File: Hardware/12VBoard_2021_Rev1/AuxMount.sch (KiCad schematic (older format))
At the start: 27 parts, among them Q4 CSD18537NQ5A, Q5 CSD18531Q5A, U10 LM5116, U11 INA198

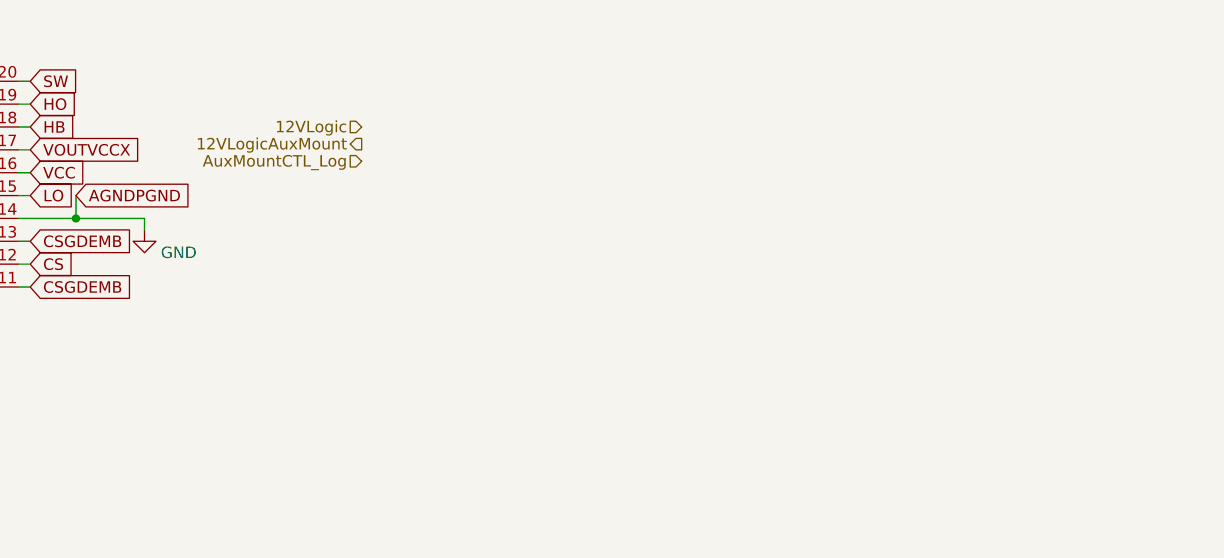
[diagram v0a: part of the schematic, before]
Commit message: Added Mosfet cicuitry to turn on/off logic power for high current side
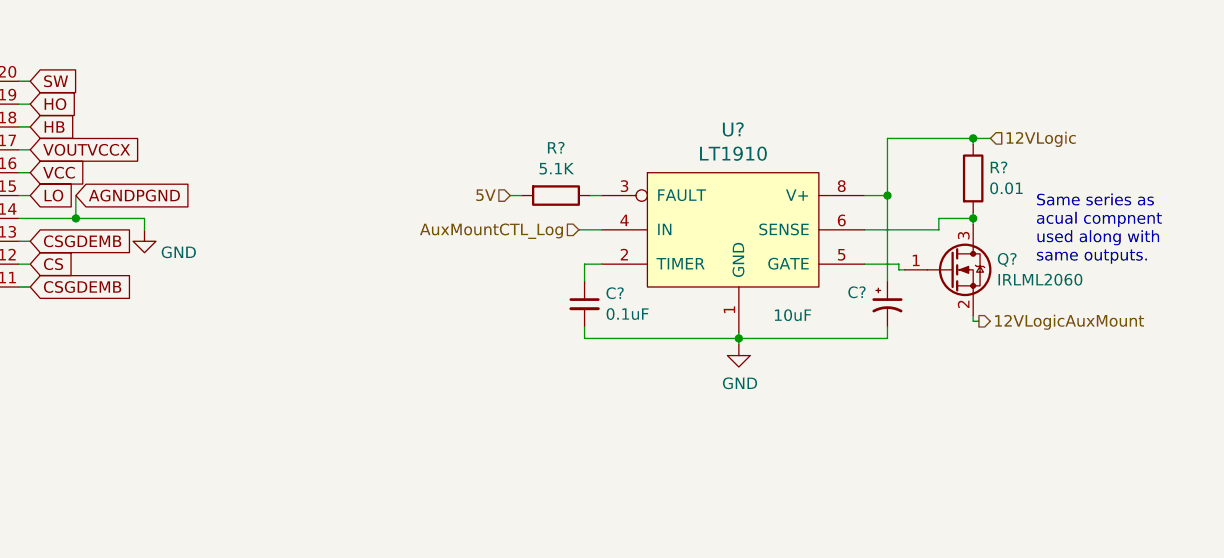
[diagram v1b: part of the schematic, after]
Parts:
- added C?: 0.1uF, symbol Device:C_Small
- added C?: 10uF, symbol Device:CP1_Small
- added Q?: IRLML2060, Package_TO_SOT_SMD:SOT-23, symbol Transistor_FET:IRLML2060
- added R?: 0.01, symbol Device:R
- added R?: 5.1K, symbol Device:R
- added U?: LT1910, symbol MRDT_ICs:LT1910
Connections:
- net 12VLogic: now also C?.1, R?.1, U?.8 (V+)
- net 12VLogicAuxMount: now also Q?.2 (S)
- net 5V: now also R?.2
- net AuxMountCTL_Log: now also U?.4 (IN)
- net GND: now also C?.2, C?.2, U?.1 (GND)
- new net: C?.1, U?.2 (TIMER)
- new net: R?.1, U?.3 (FAULT)
- new net: Q?.1 (G), U?.5 (GATE)
- new net: Q?.3 (D), R?.2, U?.6 (SENSE)
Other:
- note added: "Same series as \nacual compnent\nused along with\nsame outputs."
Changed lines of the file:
@@
 Wire Wire Line
 	1000 1100 1000 1175
-Text HLabel 5000 1000 0    50   Input ~ 0
+Text HLabel 7700 1850 2    50   Output ~ 0
+12VLogicAuxMount
+Text HLabel 5950 1450 0    50   Input ~ 0
+AuxMountCTL_Log
+Text HLabel 7750 1050 2    50   Input ~ 0
 12VLogic
-Text HLabel 5000 1075 0    50   Output ~ 0
-12VLogicAuxMount
-Text HLabel 5000 1150 0    50   Input ~ 0
-AuxMountCTL_Log
+$Comp
+L MRDT_ICs:LT1910 U?
+U 1 1 5FC2DAD4
+P 6250 1700
+AR Path="/5F74F36B/5F971CD6/5FC2DAD4" Ref="U?"  Part="1"
+AR Path="/5F74F36B/5F8222BE/5FC2DAD4" Ref="U?"  Part="1"
+F 0 "U?" H 6625 2387 60  0000 C CNN
+F 1 "LT1910" H 6625 2281 60  0000 C CNN
+F 2 "" H 6250 1700 60  0001 C CNN
+F 3 "" H 6250 1700 60  0001 C CNN
+	1    6250 1700
+	1    0    0    -1
+$EndComp
+$Comp
+L Device:C_Small C?
+U 1 1 5FC2DADA
+P 5975 1775
+AR Path="/5F74F36B/5F971CD6/5FC2DADA" Ref="C?"  Part="1"
+AR Path="/5F74F36B/5F8222BE/5FC2DADA" Ref="C?"  Part="1"
+F 0 "C?" H 6067 1821 50  0000 L CNN
+F 1 "0.1uF" H 6067 1730 50  0000 L CNN
+F 2 "" H 5975 1775 50  0001 C CNN
+F 3 "~" H 5975 1775 50  0001 C CNN
+	1    5975 1775
+	1    0    0    -1
+$EndComp
+$Comp
+L Device:CP1_Small C?
+U 1 1 5FC2DAE0
+P 7300 1775
+AR Path="/5F74F36B/5F971CD6/5FC2DAE0" Ref="C?"  Part="1"
+AR Path="/5F74F36B/5F8222BE/5FC2DAE0" Ref="C?"  Part="1"
+F 0 "C?" H 7125 1825 50  0000 L CNN
+F 1 "10uF" H 6800 1725 50  0000 L CNN
+F 2 "" H 7300 1775 50  0001 C CNN
+F 3 "~" H 7300 1775 50  0001 C CNN
+	1    7300 1775
+	1    0    0    -1
+$EndComp
+$Comp
+L power:GND #PWR?
+U 1 1 5FC2DAE6
+P 6650 1950
+AR Path="/5F74F36B/5F971CD6/5FC2DAE6" Ref="#PWR?"  Part="1"
+AR Path="/5F74F36B/5F8222BE/5FC2DAE6" Ref="#PWR?"  Part="1"
+F 0 "#PWR?" H 6650 1700 50  0001 C CNN
+F 1 "GND" H 6655 1777 50  0000 C CNN
+F 2 "" H 6650 1950 50  0001 C CNN
+F 3 "" H 6650 1950 50  0001 C CNN
+	1    6650 1950
+	1    0    0    -1
+$EndComp
+Wire Wire Line
+	6650 1900 6650 1925
+Wire Wire Line
+	6650 1950 6650 1925
+Connection ~ 6650 1925
+Wire Wire Line
+	6650 1925 5975 1925
+Wire Wire Line
+	5975 1925 5975 1875
+Wire Wire Line
+	7300 1875 7300 1925
+Wire Wire Line
+	6650 1925 7300 1925
+Wire Wire Line
+	7300 1675 7300 1300
+Wire Wire Line
+	7300 1300 7200 1300
+Wire Wire Line
+	6050 1600 5975 1600
+Wire Wire Line
+	5975 1600 5975 1675
+Wire Wire Line
+	6000 1300 6050 1300
+$Comp
+L Transistor_FET:IRLML2060 Q?
+U 1 1 5FC2DB00
+P 7575 1625
+AR Path="/5F74F36B/5F971CD6/5FC2DB00" Ref="Q?"  Part="1"
+AR Path="/5F74F36B/5F8222BE/5FC2DB00" Ref="Q?"  Part="1"
+F 0 "Q?" H 7779 1671 50  0000 L CNN
+F 1 "IRLML2060" H 7779 1580 50  0000 L CNN
+F 2 "Package_TO_SOT_SMD:SOT-23" H 7775 1550 50  0001 L CIN
+F 3 "https://www.infineon.com/dgdl/irlml2060pbf.pdf?fileId=5546d462533600a401535664b7fb25ee" H 7575 1625 50  0001 L CNN
+	1    7575 1625
+	1    0    0    -1
+$EndComp
+Wire Wire Line
+	7200 1450 7525 1450
+Wire Wire Line
+	7525 1450 7525 1400
+Wire Wire Line
+	7525 1400 7675 1400
+Wire Wire Line
+	7675 1400 7675 1375
+Wire Wire Line
+	7675 1400 7675 1425
+Connection ~ 7675 1400
+Wire Wire Line
+	7300 1300 7300 1050
+Wire Wire Line
+	7300 1050 7675 1050
+Wire Wire Line
+	7675 1050 7675 1075
+Connection ~ 7300 1300
+Wire Wire Line
+	7700 1850 7675 1850
+Wire Wire Line
+	7675 1850 7675 1825
+Connection ~ 7675 1050
+Wire Wire Line
+	7675 1050 7750 1050
+Wire Wire Line
+	5950 1450 6050 1450
+Wire Wire Line
+	7375 1625 7350 1625
+Wire Wire Line
+	7350 1625 7350 1600
+Wire Wire Line
+	7350 1600 7200 1600
+Text Notes 7950 1600 0    50   ~ 0
+Same series as \nacual compnent\nused along with\nsame outputs.
+$Comp
+L Device:R R?
+U 1 1 5FC2DB1B
+P 7675 1225
+AR Path="/5F74F36B/5F971CD6/5FC2DB1B" Ref="R?"  Part="1"
+AR Path="/5F74F36B/5F8222BE/5FC2DB1B" Ref="R?"  Part="1"
+F 0 "R?" H 7745 1271 50  0000 L CNN
+F 1 "0.01" H 7745 1180 50  0000 L CNN
+F 2 "" V 7605 1225 50  0001 C CNN
+F 3 "~" H 7675 1225 50  0001 C CNN
+	1    7675 1225
+	1    0    0    -1
+$EndComp
+$Comp
+L Device:R R?
+U 1 1 5FC2DB21
+P 5850 1300
+AR Path="/5F74F36B/5F971CD6/5FC2DB21" Ref="R?"  Part="1"
+AR Path="/5F74F36B/5F8222BE/5FC2DB21" Ref="R?"  Part="1"
+F 0 "R?" V 5643 1300 50  0000 C CNN
+F 1 "5.1K" V 5734 1300 50  0000 C CNN
+F 2 "" V 5780 1300 50  0001 C CNN
+F 3 "~" H 5850 1300 50  0001 C CNN
+	1    5850 1300
+	0    1    1    0
+$EndComp
+Text HLabel 5650 1300 0    50   Input ~ 0
+5V
+Wire Wire Line
+	5650 1300 5700 1300
 $EndSCHEMATC

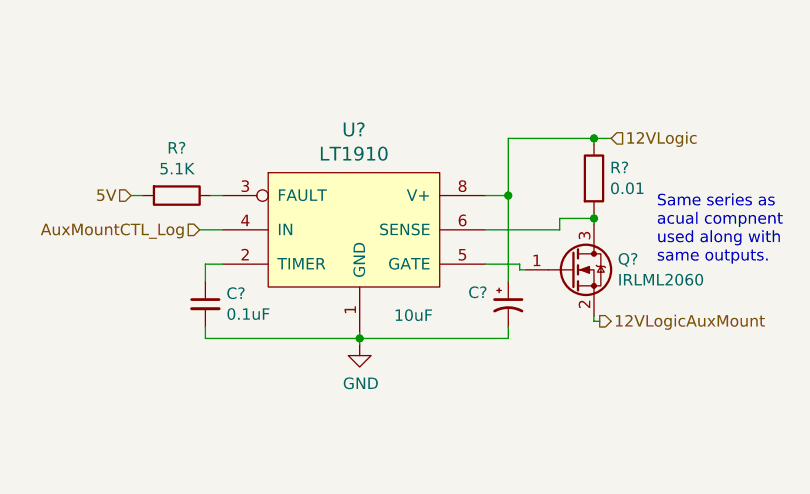
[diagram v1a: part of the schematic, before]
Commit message: Redesigned low current ports schematic
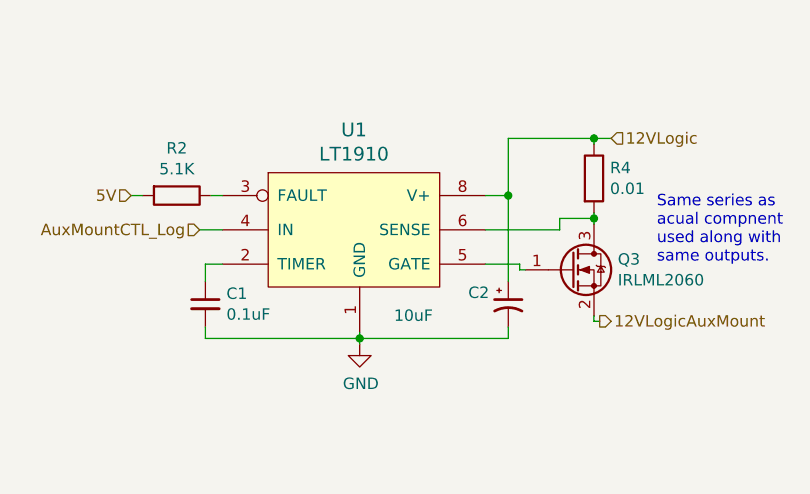
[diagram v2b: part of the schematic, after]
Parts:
- gave numbers to parts that had none: 6
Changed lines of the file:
@@
 P 6250 1700
 AR Path="/5F74F36B/5F971CD6/5FC2DAD4" Ref="U?"  Part="1"
-AR Path="/5F74F36B/5F8222BE/5FC2DAD4" Ref="U?"  Part="1"
-F 0 "U?" H 6625 2387 60  0000 C CNN
+AR Path="/5F74F36B/5F8222BE/5FC2DAD4" Ref="U1"  Part="1"
+F 0 "U1" H 6625 2387 60  0000 C CNN
 F 1 "LT1910" H 6625 2281 60  0000 C CNN
 F 2 "" H 6250 1700 60  0001 C CNN
@@
 P 5975 1775
 AR Path="/5F74F36B/5F971CD6/5FC2DADA" Ref="C?"  Part="1"
-AR Path="/5F74F36B/5F8222BE/5FC2DADA" Ref="C?"  Part="1"
-F 0 "C?" H 6067 1821 50  0000 L CNN
+AR Path="/5F74F36B/5F8222BE/5FC2DADA" Ref="C1"  Part="1"
+F 0 "C1" H 6067 1821 50  0000 L CNN
 F 1 "0.1uF" H 6067 1730 50  0000 L CNN
 F 2 "" H 5975 1775 50  0001 C CNN
@@
 P 7300 1775
 AR Path="/5F74F36B/5F971CD6/5FC2DAE0" Ref="C?"  Part="1"
-AR Path="/5F74F36B/5F8222BE/5FC2DAE0" Ref="C?"  Part="1"
-F 0 "C?" H 7125 1825 50  0000 L CNN
+AR Path="/5F74F36B/5F8222BE/5FC2DAE0" Ref="C2"  Part="1"
+F 0 "C2" H 7125 1825 50  0000 L CNN
 F 1 "10uF" H 6800 1725 50  0000 L CNN
 F 2 "" H 7300 1775 50  0001 C CNN
@@
 P 6650 1950
 AR Path="/5F74F36B/5F971CD6/5FC2DAE6" Ref="#PWR?"  Part="1"
-AR Path="/5F74F36B/5F8222BE/5FC2DAE6" Ref="#PWR?"  Part="1"
-F 0 "#PWR?" H 6650 1700 50  0001 C CNN
+AR Path="/5F74F36B/5F8222BE/5FC2DAE6" Ref="#PWR01"  Part="1"
+F 0 "#PWR01" H 6650 1700 50  0001 C CNN
 F 1 "GND" H 6655 1777 50  0000 C CNN
 F 2 "" H 6650 1950 50  0001 C CNN
@@
 P 7575 1625
 AR Path="/5F74F36B/5F971CD6/5FC2DB00" Ref="Q?"  Part="1"
-AR Path="/5F74F36B/5F8222BE/5FC2DB00" Ref="Q?"  Part="1"
-F 0 "Q?" H 7779 1671 50  0000 L CNN
+AR Path="/5F74F36B/5F8222BE/5FC2DB00" Ref="Q3"  Part="1"
+F 0 "Q3" H 7779 1671 50  0000 L CNN
 F 1 "IRLML2060" H 7779 1580 50  0000 L CNN
 F 2 "Package_TO_SOT_SMD:SOT-23" H 7775 1550 50  0001 L CIN
@@
 P 7675 1225
 AR Path="/5F74F36B/5F971CD6/5FC2DB1B" Ref="R?"  Part="1"
-AR Path="/5F74F36B/5F8222BE/5FC2DB1B" Ref="R?"  Part="1"
-F 0 "R?" H 7745 1271 50  0000 L CNN
+AR Path="/5F74F36B/5F8222BE/5FC2DB1B" Ref="R4"  Part="1"
+F 0 "R4" H 7745 1271 50  0000 L CNN
 F 1 "0.01" H 7745 1180 50  0000 L CNN
 F 2 "" V 7605 1225 50  0001 C CNN
@@
 P 5850 1300
 AR Path="/5F74F36B/5F971CD6/5FC2DB21" Ref="R?"  Part="1"
-AR Path="/5F74F36B/5F8222BE/5FC2DB21" Ref="R?"  Part="1"
-F 0 "R?" V 5643 1300 50  0000 C CNN
+AR Path="/5F74F36B/5F8222BE/5FC2DB21" Ref="R2"  Part="1"
+F 0 "R2" V 5643 1300 50  0000 C CNN
 F 1 "5.1K" V 5734 1300 50  0000 C CNN
 F 2 "" V 5780 1300 50  0001 C CNN

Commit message: Layed out logic power
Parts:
- C1: footprint (none) -> Capacitor_SMD:C_0603_1608Metric_Pad1.05x0.95mm_HandSolder
- C2: footprint (none) -> Capacitor_THT:CP_Radial_D5.0mm_P2.00mm
- R2, R4: footprint (none) -> Resistor_SMD:R_0603_1608Metric_Pad1.05x0.95mm_HandSolder
- U1: footprint (none) -> Package_SO:SOIC-8-N7_3.9x4.9mm_P1.27mm
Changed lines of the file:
@@
 F 0 "U1" H 6625 2387 60  0000 C CNN
 F 1 "LT1910" H 6625 2281 60  0000 C CNN
-F 2 "" H 6250 1700 60  0001 C CNN
+F 2 "Package_SO:SOIC-8-N7_3.9x4.9mm_P1.27mm" H 6250 1700 60  0001 C CNN
 F 3 "" H 6250 1700 60  0001 C CNN
 	1    6250 1700
@@
 F 0 "C1" H 6067 1821 50  0000 L CNN
 F 1 "0.1uF" H 6067 1730 50  0000 L CNN
-F 2 "" H 5975 1775 50  0001 C CNN
+F 2 "Capacitor_SMD:C_0603_1608Metric_Pad1.05x0.95mm_HandSolder" H 5975 1775 50  0001 C CNN
 F 3 "~" H 5975 1775 50  0001 C CNN
 	1    5975 1775
@@
 F 0 "C2" H 7125 1825 50  0000 L CNN
 F 1 "10uF" H 6800 1725 50  0000 L CNN
-F 2 "" H 7300 1775 50  0001 C CNN
+F 2 "Capacitor_THT:CP_Radial_D5.0mm_P2.00mm" H 7300 1775 50  0001 C CNN
 F 3 "~" H 7300 1775 50  0001 C CNN
 	1    7300 1775
@@
 F 0 "R4" H 7745 1271 50  0000 L CNN
 F 1 "0.01" H 7745 1180 50  0000 L CNN
-F 2 "" V 7605 1225 50  0001 C CNN
+F 2 "Resistor_SMD:R_0603_1608Metric_Pad1.05x0.95mm_HandSolder" V 7605 1225 50  0001 C CNN
 F 3 "~" H 7675 1225 50  0001 C CNN
 	1    7675 1225
@@
 F 0 "R2" V 5643 1300 50  0000 C CNN
 F 1 "5.1K" V 5734 1300 50  0000 C CNN
-F 2 "" V 5780 1300 50  0001 C CNN
+F 2 "Resistor_SMD:R_0603_1608Metric_Pad1.05x0.95mm_HandSolder" V 5780 1300 50  0001 C CNN
 F 3 "~" H 5850 1300 50  0001 C CNN
 	1    5850 1300

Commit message: Started layout of bucks
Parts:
- L7: footprint Inductor_SMD:L_0603_1608Metric_Pad1.05x0.95mm_HandSolder -> MRDT_12VoltBoard:IND_SER2915L-682KL
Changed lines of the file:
@@
 F 0 "L7" V 1535 3600 50  0000 C CNN
 F 1 "6.6uH 1.5m" V 1444 3600 50  0000 C CNN
-F 2 "Inductor_SMD:L_0603_1608Metric_Pad1.05x0.95mm_HandSolder" H 1350 3600 50  0001 C CNN
+F 2 "MRDT_12VoltBoard:IND_SER2915L-682KL" H 1350 3600 50  0001 C CNN
 F 3 "~" H 1350 3600 50  0001 C CNN
 	1    1350 3600

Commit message: found Big inductors
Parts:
- L7: value 6.6uH 1.5m -> 10uH; footprint MRDT_12VoltBoard:IND_SER2915L-682KL -> Inductor_THT:L_Radial_D27.9mm_P20.07mm_Vishay_IHB-3
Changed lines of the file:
@@
 AR Path="/5F74F36B/5F8222BE/5FE33034" Ref="L7"  Part="1"
 F 0 "L7" V 1535 3600 50  0000 C CNN
-F 1 "6.6uH 1.5m" V 1444 3600 50  0000 C CNN
-F 2 "MRDT_12VoltBoard:IND_SER2915L-682KL" H 1350 3600 50  0001 C CNN
+F 1 "10uH" V 1444 3600 50  0000 C CNN
+F 2 "Inductor_THT:L_Radial_D27.9mm_P20.07mm_Vishay_IHB-3" H 1350 3600 50  0001 C CNN
 F 3 "~" H 1350 3600 50  0001 C CNN
 	1    1350 3600

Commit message: Added all logic circuits for high current
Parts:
- R25: footprint Resistor_SMD:R_2512_6332Metric_Pad1.52x3.35mm_HandSolder -> Package_TO_SOT_THT:TO-126-2_Vertical
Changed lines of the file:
@@
 F 0 "R25" V 3093 3600 50  0000 C CNN
 F 1 "50m" V 3184 3600 50  0000 C CNN
-F 2 "Resistor_SMD:R_2512_6332Metric_Pad1.52x3.35mm_HandSolder" V 3230 3600 50  0001 C CNN
+F 2 "Package_TO_SOT_THT:TO-126-2_Vertical" V 3230 3600 50  0001 C CNN
 F 3 "~" H 3300 3600 50  0001 C CNN
 	1    3300 3600

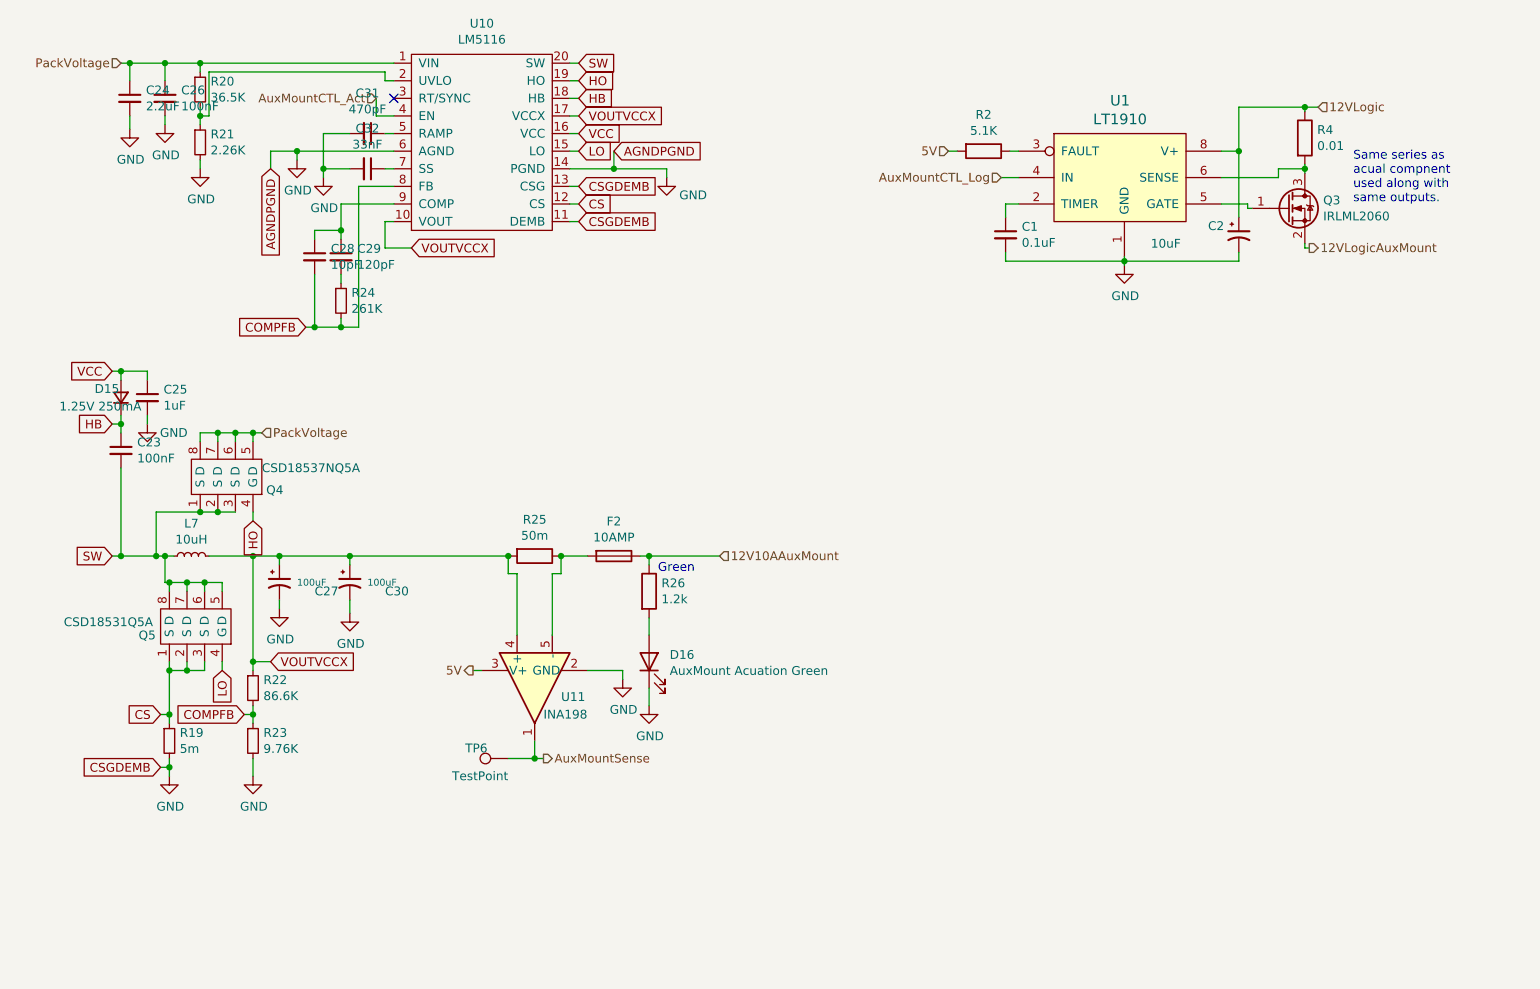
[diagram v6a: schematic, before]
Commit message: changed to big bucks
changed to the bucks used in Master due to a realization in the inductor sizing for the LM5116. It would be much bigger than previous years.
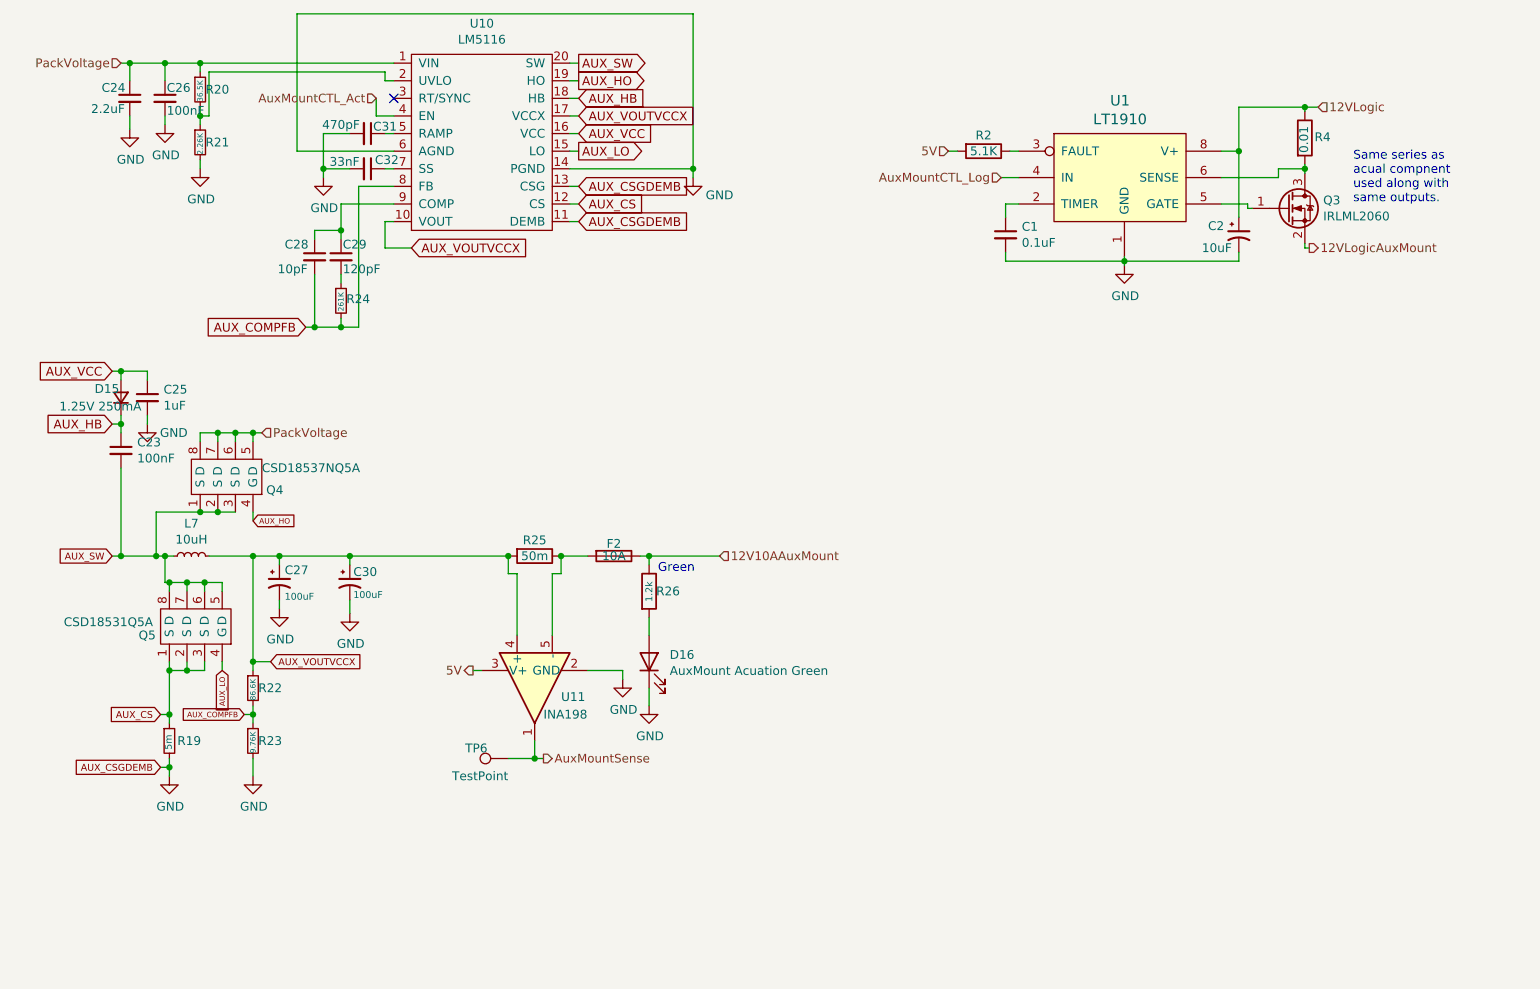
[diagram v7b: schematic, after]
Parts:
- F2: value 10AMP -> 10A
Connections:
- net COMPFB renamed AUX_COMPFB
- net CS renamed AUX_CS
- net HB renamed AUX_HB
- net HO renamed AUX_HO
- net LO renamed AUX_LO
- net SW renamed AUX_SW
- net VCC renamed AUX_VCC
- net VOUTVCCX renamed AUX_VOUTVCCX
